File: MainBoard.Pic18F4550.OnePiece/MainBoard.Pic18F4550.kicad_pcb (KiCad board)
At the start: 2 copper layers, 83 parts, among them CON1 USB_CON, J1 VIKING_CON_9P, J10 IO_CON_8P, J11 PORTB_CON_6P, J12 PORTCD_CON_5P, J13 PORTA_CON_7P, J2 GPIB_CON_9P, J3 VIKING_CON_9P, J4 GPIB_CON_9P, J5 POWER_CON_01X06, J6 VIKING_CON_01X09, J7 VIKING_CON_01X09, J8 RESET_CON_01X02, J9 IO_CON_8P, U1 PCA6416A, U2 PIC18F4550-I/P, U3 MC33996EKR2, U4 MC33996EKR2, U5 PCA6416A, Y1 20MHZ

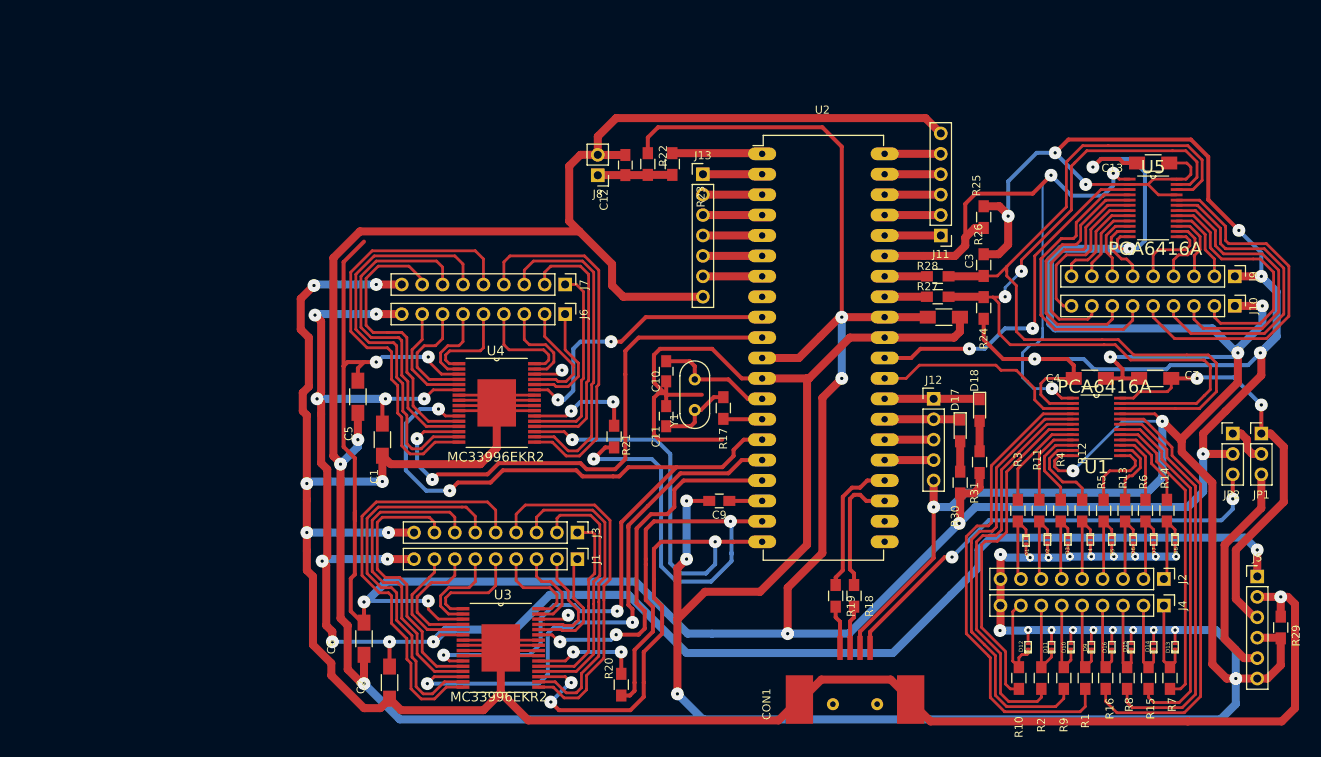
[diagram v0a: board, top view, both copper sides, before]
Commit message: Revision de PCBs + MergedPcbs
  - Se revisan PCBs
      - VikingPortExpander
      - GpibPortExpander
      - MainBoards en tres versiones
  - Se genera archivos Gerber que combina estos PCBs en un documento
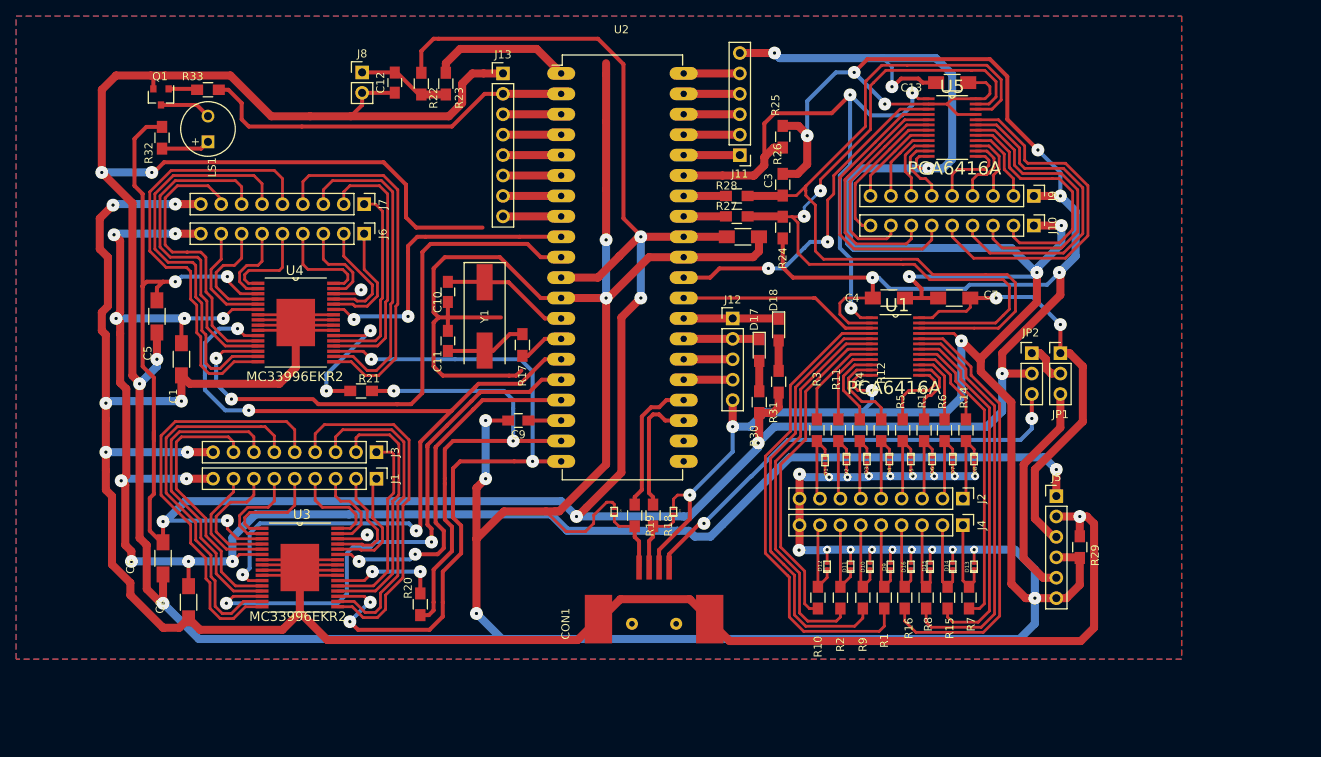
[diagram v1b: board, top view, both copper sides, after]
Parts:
- added D19: SP1003, CenditFootprints:SP1003-01ETG, F.Cu at (151.8, 116.6)
- added D20: SP1003, CenditFootprints:SP1003-01ETG, F.Cu at (144.4, 116.6)
- added LS1: Speaker, Buzzers_Beepers:MagneticBuzzer_Kingstate_KCG0601, F.Cu at (93.9, 70.6)
- added Q1: 2N3904, TO_SOT_Packages_SMD:SOT-23, F.Cu at (88.0, 65.1)
- added R32: 1k, Resistors_SMD:R_0805_HandSoldering, F.Cu at (88.2, 70.1)
- added R33: 10k, Resistors_SMD:R_0805_HandSoldering, F.Cu at (93.9, 64.2)
- J13: value PORTA_CON_7P -> PORTAE_CON_8P; footprint Pin_Headers:Pin_Header_Straight_1x07_Pitch2.54mm -> Pin_Headers:Pin_Header_Straight_1x08_Pitch2.54mm
- Y1: footprint Crystals:Crystal_HC52-6mm_Vertical -> Crystals:Crystal_SMD_HC49-SD
- moved J8 32.0 mm to (113.0, 62.0), turned to 0 degrees
- moved R21 32.0 mm to (112.9, 101.6), turned to 180 degrees
- moved C12 30.5 mm to (117.1, 63.3), turned to 270 degrees
- moved R23 29.9 mm to (123.5, 63.4)
- moved R22 29.9 mm to (120.4, 63.4)
- moved C10 28.9 mm to (123.7, 89.3)
- moved C11 28.7 mm to (123.7, 95.4)
- moved J13 27.9 mm to (130.6, 62.1)
- moved Y1 27.3 mm to (128.3, 92.4)
- moved R20 26.9 mm to (120.3, 128.2)
- moved U4 26.9 mm to (104.8, 93.1)
- moved C1 26.9 mm to (90.6, 97.7)
- moved C2 26.9 mm to (91.5, 127.9)
- moved C3 26.9 mm to (160.4, 82.5)
- moved C4 26.9 mm to (178.6, 90.1)
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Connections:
- net /PD4 renamed PD4
- net /PD5 renamed PD5
- net Net-(CON1-Pad2) renamed D-
- net Net-(CON1-Pad3) renamed D+
- J13 pad 1: /PA0 -> GND
- J13 pad 2: /PA1 -> PA0
- J13 pad 3: /PA2 -> /PA1
- J13 pad 4: /PA3 -> /PA2
- J13 pad 5: /PA4 -> /PA3
- J13 pad 6: /PA5 -> /PA4
- J13 pad 7: GND -> /PA5
- U2 pad 2: /PA0 -> PA0
- U2 pad 8: (no net) -> /PE0
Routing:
- net GND: track 789.5 -> 879.1 mm, vias 33 -> 39
- net PA0: track 0.00 -> 47.6 mm
- net /MISO: track 78.1 -> 61.3 mm
- net /PA0: track 7.37 -> 0.00 mm
- net /PE0: track 0.00 -> 7.24 mm
- net MCLR: track 11.2 -> 17.8 mm
- net Net-(LS1-Pad2): track 0.00 -> 6.42 mm
- net Net-(LS1-Pad1): track 0.00 -> 6.06 mm
- net /MOSI: track 95.4 -> 91.2 mm
- net /SPI_SCLK: track 111.9 -> 107.8 mm
- net Net-(R21-Pad2): track 13.5 -> 17.5 mm
- net /U4_CS: track 68.3 -> 72.1 mm
- net D-: track 5.33 -> 9.06 mm
- net D+: track 5.35 -> 9.08 mm
- net //INT: track 78.5 -> 74.9 mm
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- added copper zone on B.Cu, net GND
- added copper zone on F.Cu, net GND
